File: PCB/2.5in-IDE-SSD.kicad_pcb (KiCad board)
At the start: 4 copper layers, 65 x 49.8 mm, 93 parts, among them J1 Conn_02x22_Odd_Even, J2 Conn_02x02_Odd_Even, U1 SM2236, U2 TLV75533PDRV, U3 FlashBGA152, U4 FlashBGA152, U5 FlashBGA152, U6 FlashBGA152, U7 TLV75518PDRV

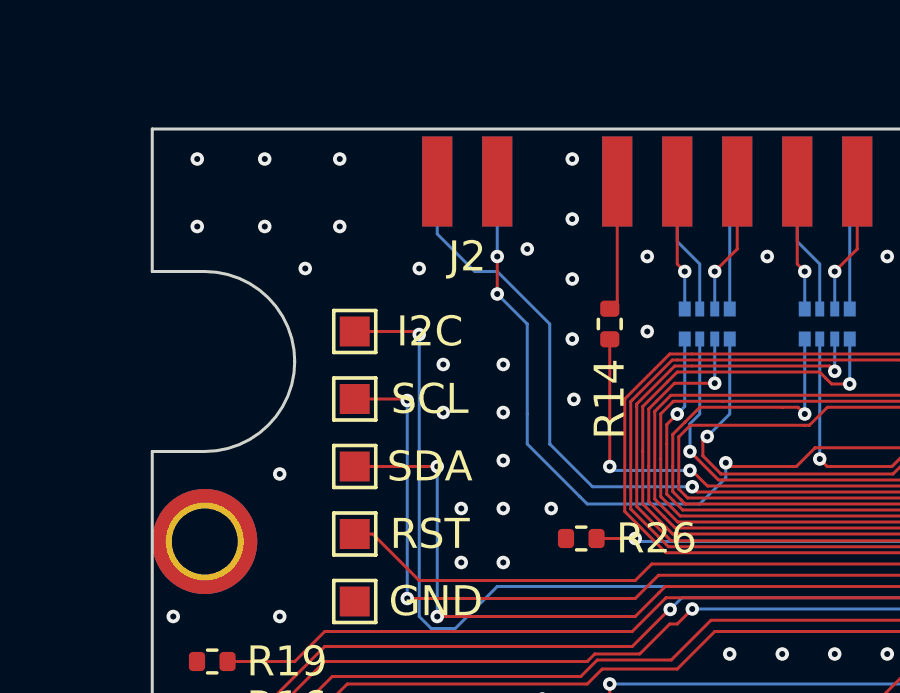
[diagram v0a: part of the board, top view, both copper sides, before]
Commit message: Reversed state of master/slave select, making master mode enabled when jumper is removed
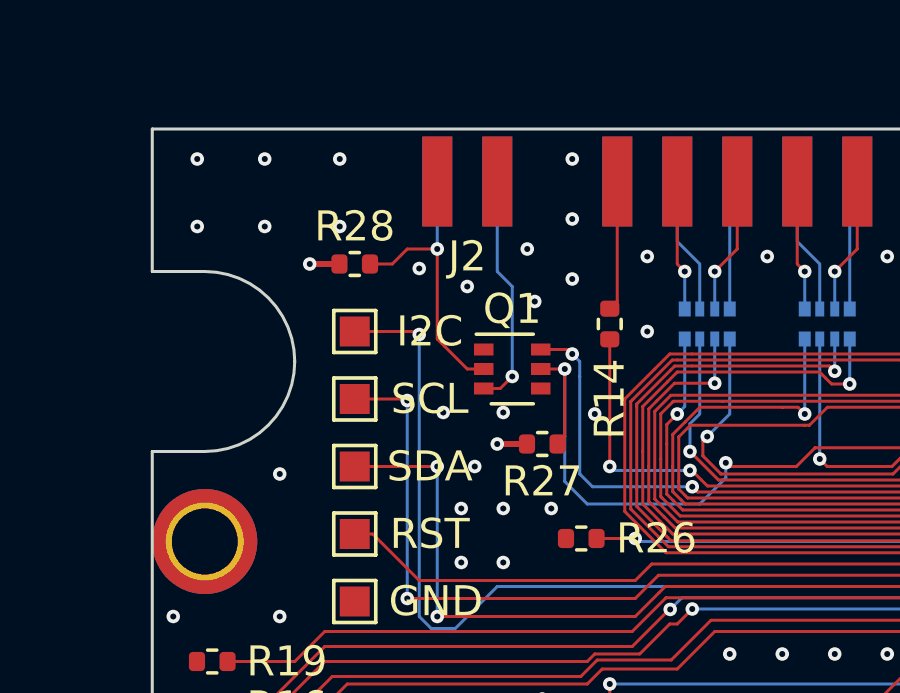
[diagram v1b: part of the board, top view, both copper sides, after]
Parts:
- added Q1: PMBT2222AYS, Package_TO_SOT_SMD:SOT-363_SC-70-6, F.Cu at (142.5, 72.8)
- added R27: 10k, Resistor_SMD:R_0402_1005Metric, F.Cu at (143.5, 75.2)
- added R28: 10k, Resistor_SMD:R_0402_1005Metric, F.Cu at (137.2, 69.2)
- C3, C5, C7, C9: value 0.12uF -> 150nF
- R15: value 300 -> 330
- U3, U4, U5, U6: footprint Package_BGA:BGA-152_14x18mm_Layout13x17_P0.5mm -> cust:BGA-152_14x18mm_Layout13x17_P0.5mm
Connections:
- J2 pad 2: /HD_CSEL# -> Net-(J2-Pad2)
- J2 pad 4: /HD_CSEL_CONN# -> Net-(J2-Pad4)
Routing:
- net Net-(J2-Pad2): track 0.00 -> 9.66 mm, vias 0 -> 1
- net Net-(J2-Pad4): track 0.00 -> 7.82 mm, vias 0 -> 1
- net /HD_CSEL#: track 35.7 -> 28.8 mm, vias 3 -> 4
- net /HD_CSEL_CONN#: track 47.7 -> 43.9 mm, vias 4 -> 3
- net +3V3: track 94.8 -> 96.8 mm, vias 48 -> 50
- net GND: vias 222 -> 220
